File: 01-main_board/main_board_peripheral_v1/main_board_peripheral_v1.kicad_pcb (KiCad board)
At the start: 2 copper layers, 53.5 x 19.7 mm, 4 parts, among them J1 T4040014041-000, J2 T4040014041-000, J3 0907790004

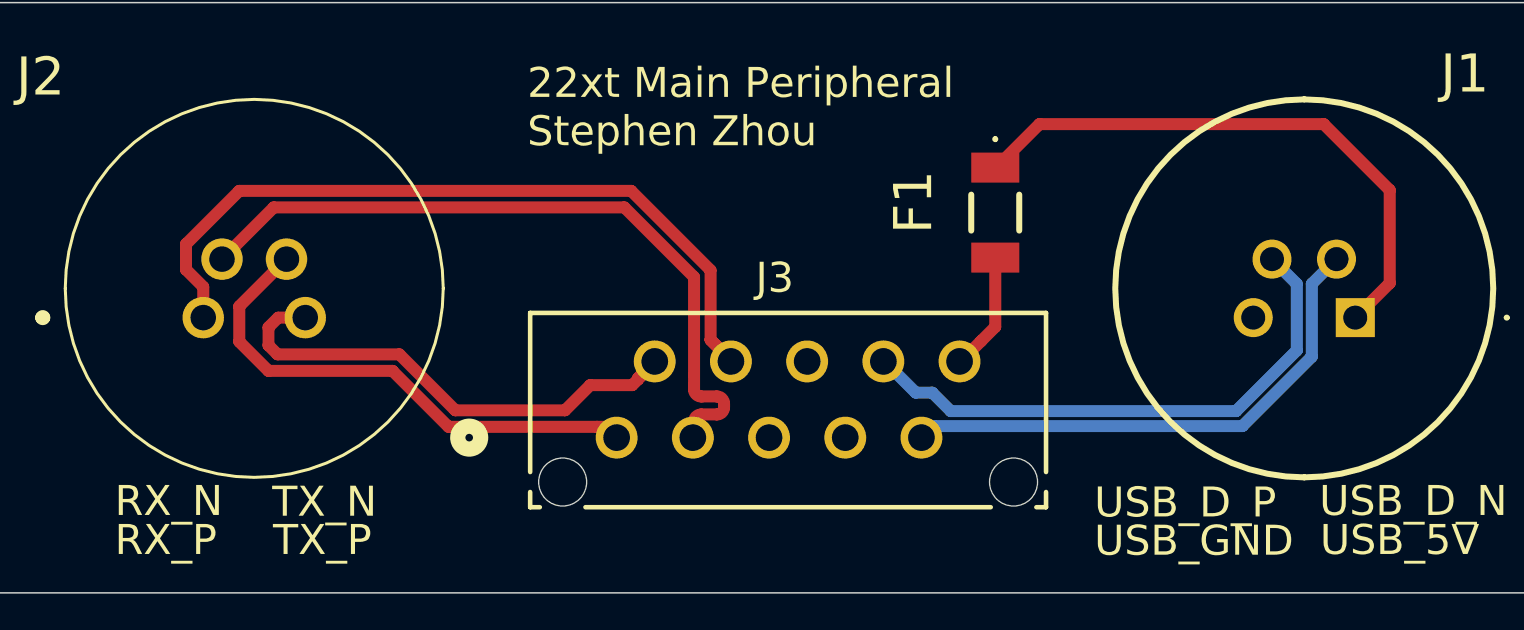
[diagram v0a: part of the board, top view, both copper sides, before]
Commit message: Redid usb ethernet diff pairing
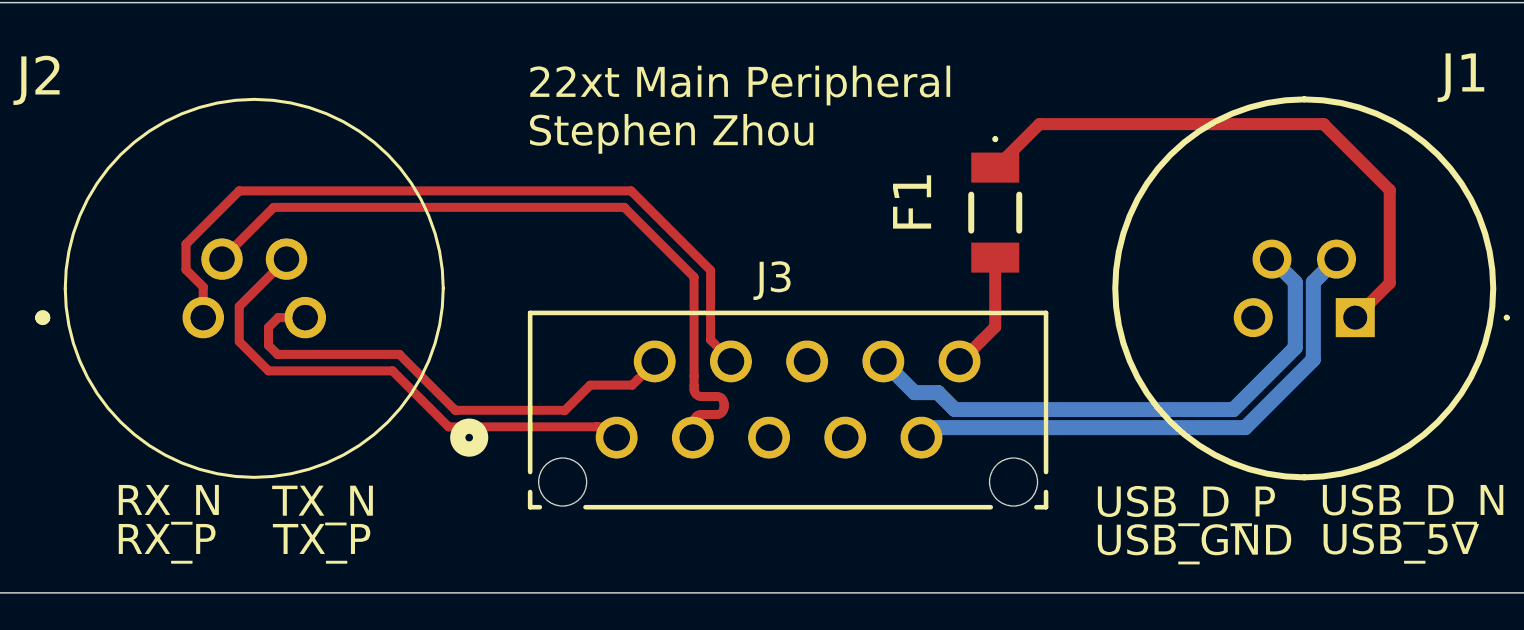
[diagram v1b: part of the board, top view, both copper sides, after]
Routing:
- net RX_P: track 26.3 -> 25.3 mm
- net TX_P: track 17.3 -> 16.4 mm
- net TX_N: track 18.4 -> 17.8 mm
